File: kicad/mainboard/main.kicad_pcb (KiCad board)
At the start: 2 copper layers, 55 x 45 mm, 38 parts, among them IC2 LM358D, IC3 MC34063AD, J1 Power, J2 GM Tube, Q1 IRF840, Q2 Q_PNP_BEC, Q3 BC848SMD, Q4 BC848SMD

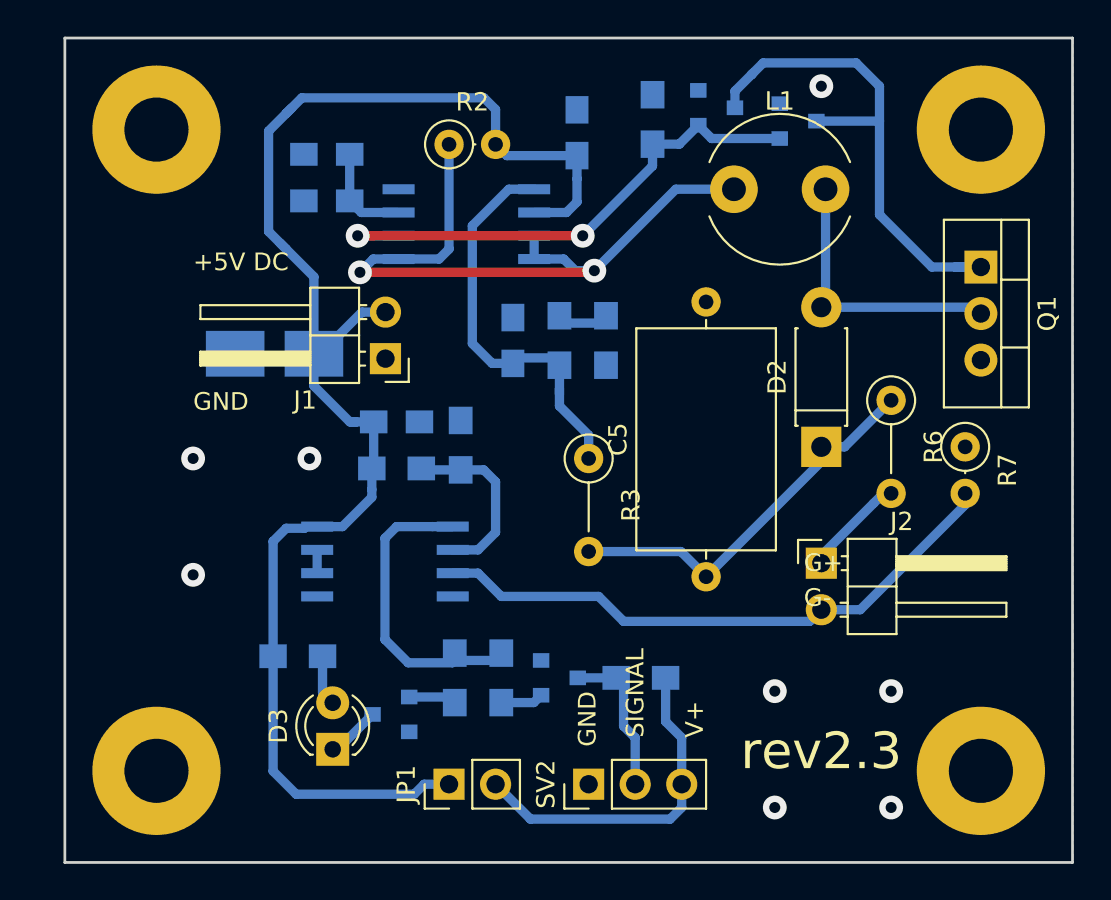
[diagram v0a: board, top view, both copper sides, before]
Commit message: directory structure change
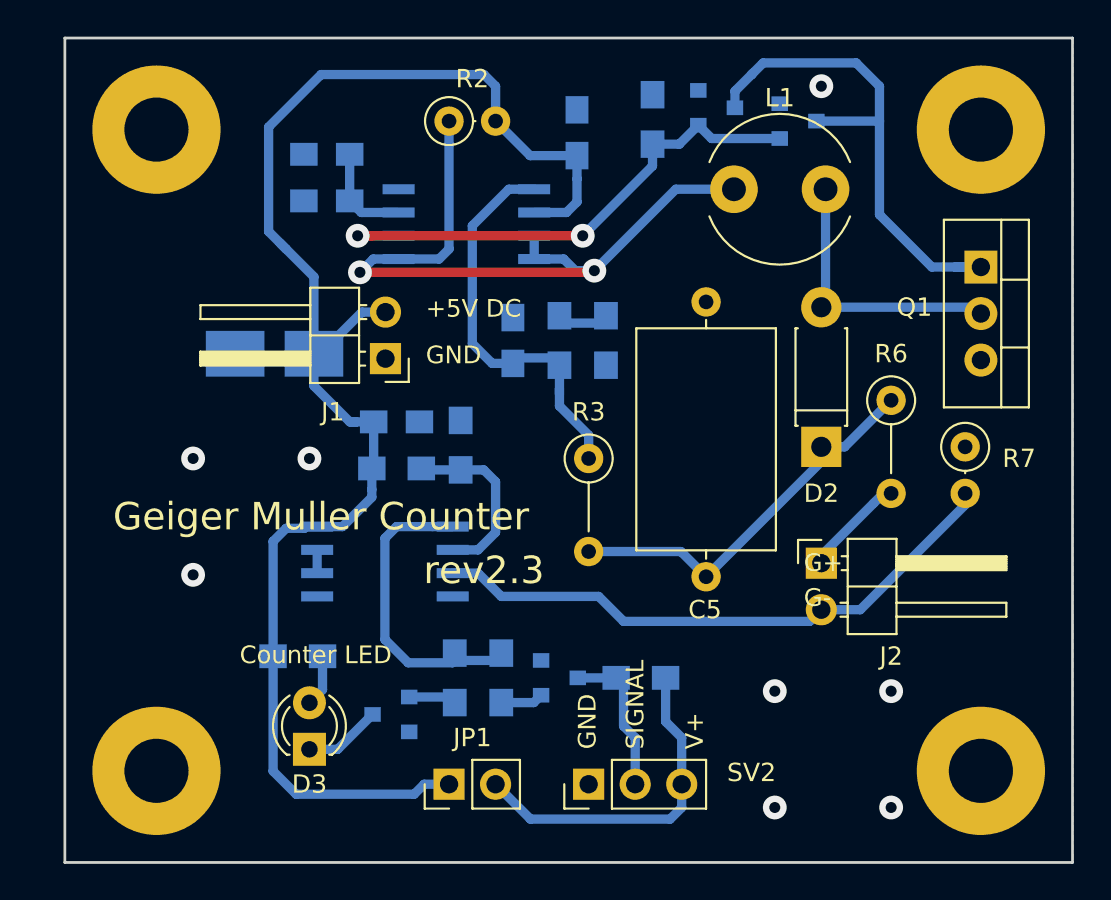
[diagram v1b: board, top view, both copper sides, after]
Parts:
- moved D3 1.27 mm to (133.3, 123.8)
- moved R2 1.27 mm to (141.0, 89.5)
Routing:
- net Net-(IC3-Pad1): track 38.2 -> 39.5 mm
- net Net-(D3-Pad1): track 2.96 -> 4.23 mm
- net Net-(C3-Pad1): track 83.9 -> 84.7 mm
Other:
- net class high voltage added: clearance 0.6, trace_width 0.508, via_dia 1.3, via_drill 0.6
- board text added: "Counter LED"
- board text added: "Geiger Muller Counter"
